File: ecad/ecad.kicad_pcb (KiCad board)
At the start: 2 copper layers, 0 parts

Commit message: chore (ecad): init PCB & Schematic
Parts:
- added U1: ESP32-CAM, boards:ESP32-CAM-DEVKIT, F.Cu at (63.5, 96.0)
- added U2: ESP32-WROOM-32, boards:ESP32-DEVKIT_CH340C, F.Cu at (70.0, 88.5)
- added U3: ESP32-WROOM-32, boards:ESP32-DEVKIT_CP2102, F.Cu at (76.5, 88.0)
- added U4: ESP32-S3, boards:ESP32-S3-DEVKIT_CH343p, F.Cu at (83.0, 86.0)

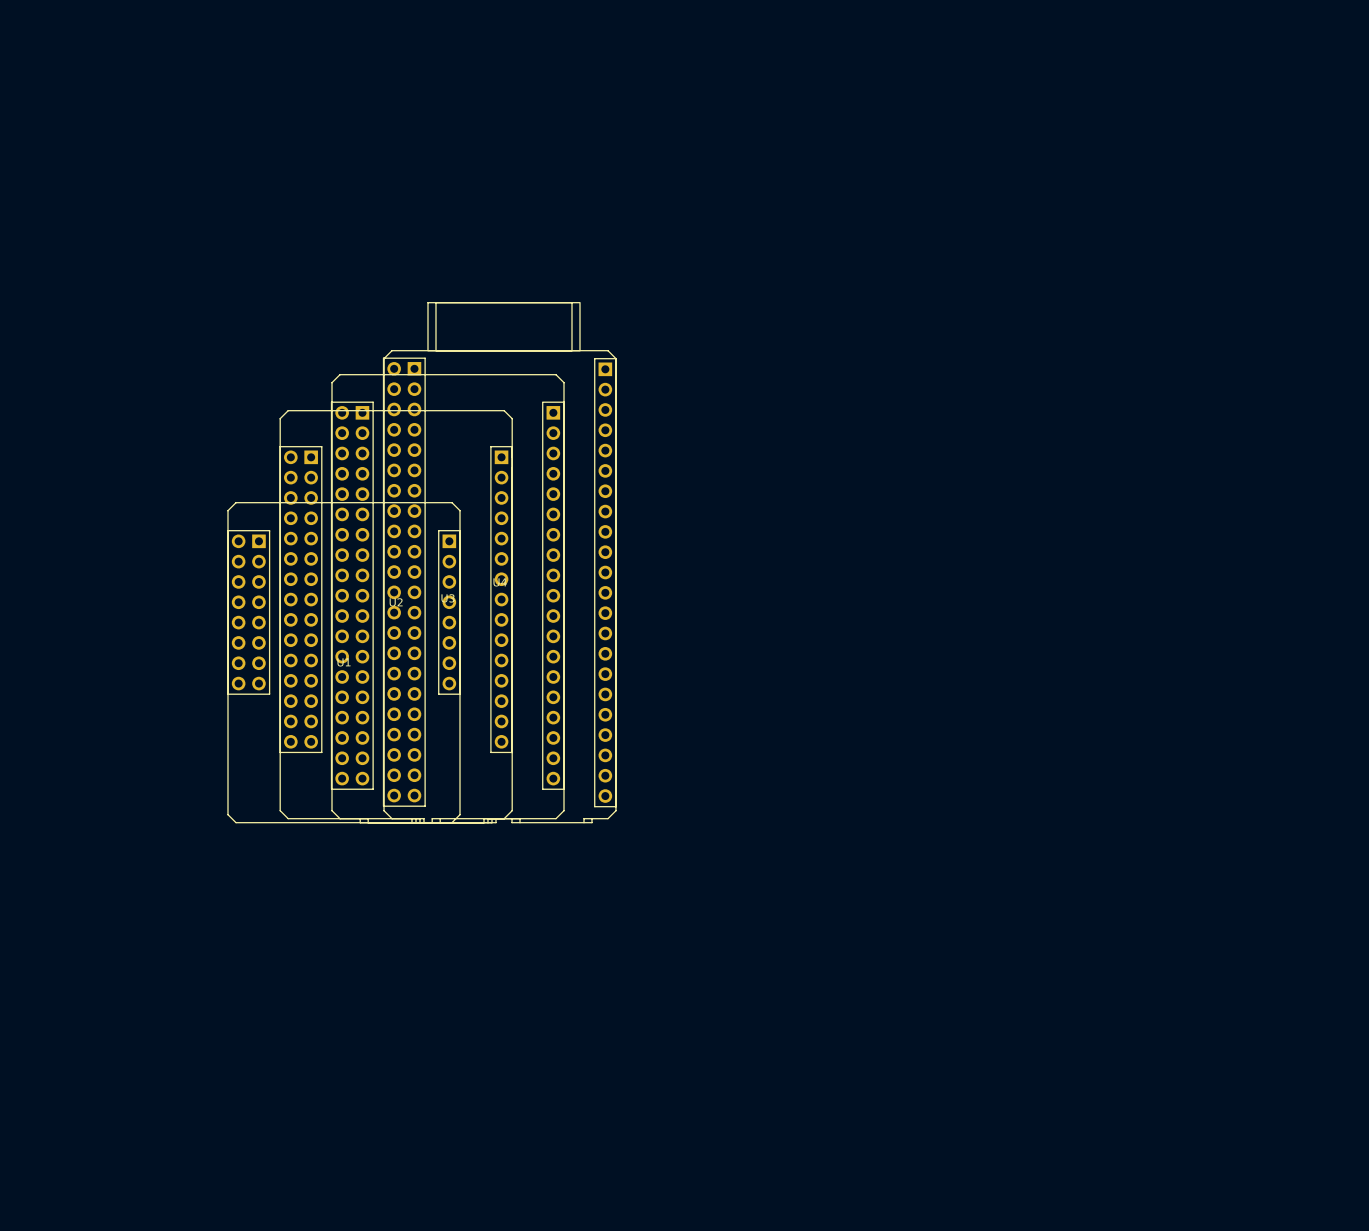
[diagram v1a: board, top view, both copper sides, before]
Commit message: feat (ecad): start PCB design
Left header pins and LEDs connected to devkits without ground-voltage
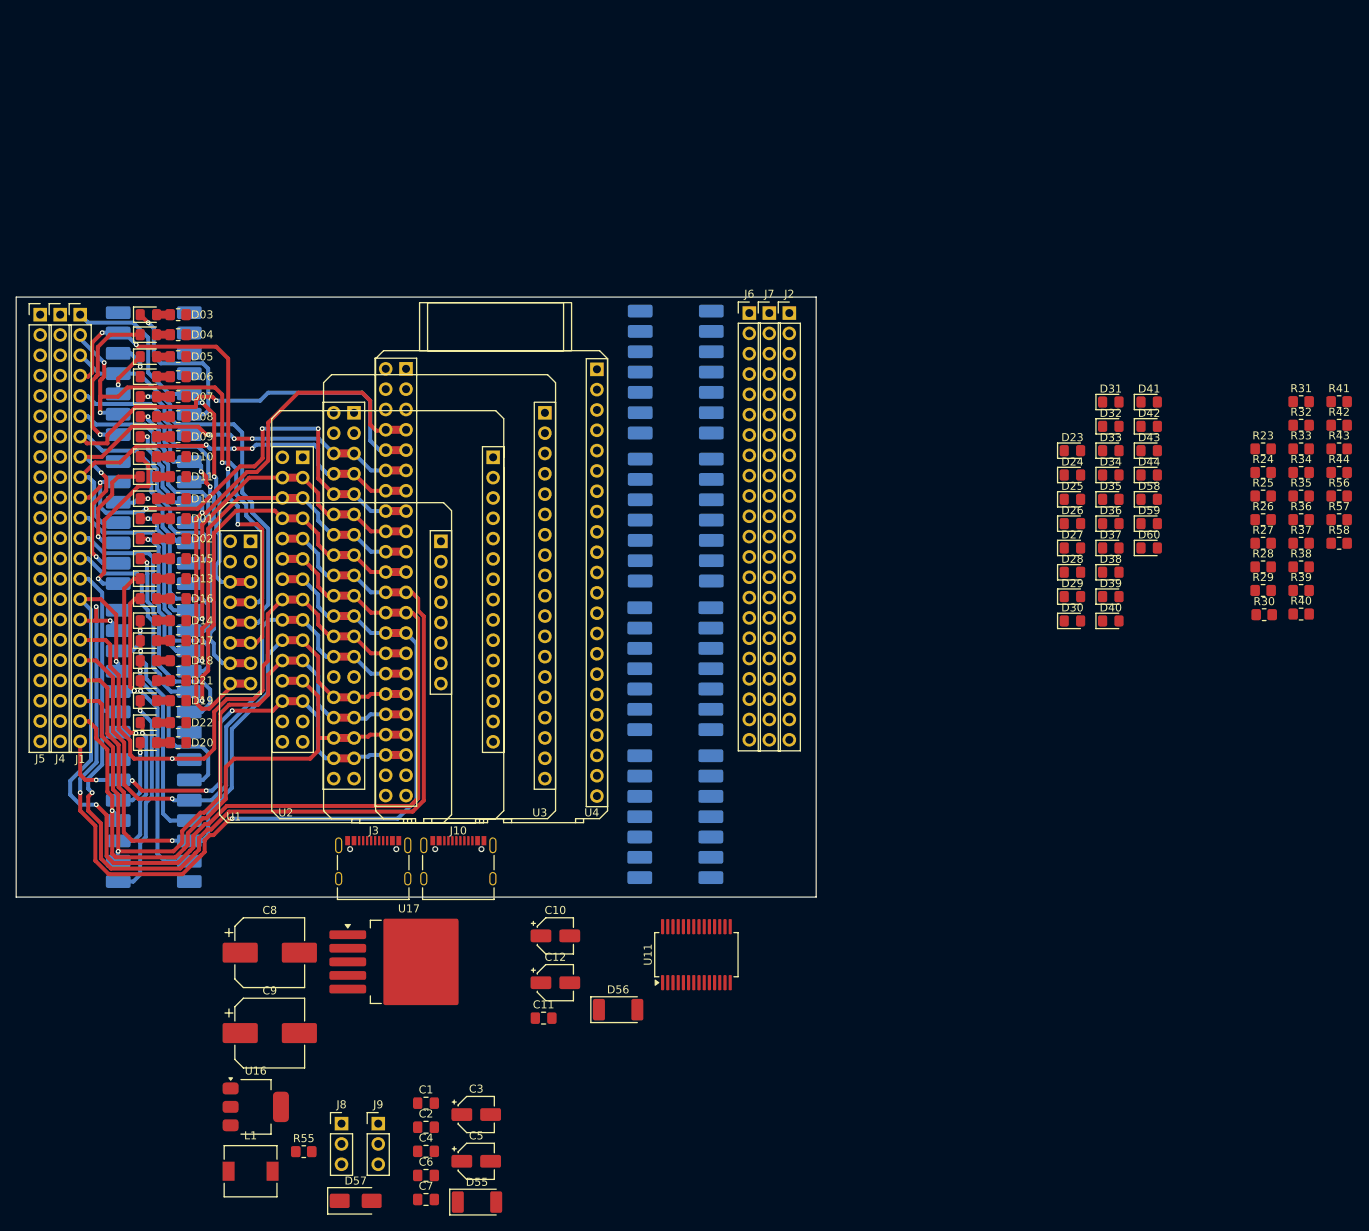
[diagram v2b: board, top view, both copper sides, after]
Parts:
- added C1: 100n, Capacitor_SMD:C_0805_2012Metric_Pad1.18x1.45mm_HandSolder, F.Cu at (73.7, 151.1)
- added C10: 1u, Capacitor_SMD:CP_Elec_4x5.4, F.Cu at (89.9, 130.2)
- added C11: 100n, Capacitor_SMD:C_0805_2012Metric_Pad1.18x1.45mm_HandSolder, F.Cu at (88.4, 140.4)
- added C12: 4.7u, Capacitor_SMD:CP_Elec_4x5.4, F.Cu at (89.9, 136.0)
- added C2: 100n, Capacitor_SMD:C_0805_2012Metric_Pad1.18x1.45mm_HandSolder, F.Cu at (73.7, 154.1)
- added C3: 1u, Capacitor_SMD:CP_Elec_4x5.4, F.Cu at (80.0, 152.5)
- added C4: 100n, Capacitor_SMD:C_0805_2012Metric_Pad1.18x1.45mm_HandSolder, F.Cu at (73.7, 157.1)
- added C5: 4.7u, Capacitor_SMD:CP_Elec_4x5.4, F.Cu at (80.0, 158.3)
- added C6: 22u, Capacitor_SMD:C_0805_2012Metric_Pad1.18x1.45mm_HandSolder, F.Cu at (73.7, 160.1)
- added C7: 22u, Capacitor_SMD:C_0805_2012Metric_Pad1.18x1.45mm_HandSolder, F.Cu at (73.7, 163.1)
- added C8: 470u, Capacitor_SMD:CP_Elec_8x10.5, F.Cu at (54.2, 132.2)
- added C9: 470u, Capacitor_SMD:CP_Elec_8x10.5, F.Cu at (54.2, 142.3)
- added D01: LED, LED_SMD:LED_0805_2012Metric_Pad1.15x1.40mm_HandSolder, F.Cu at (39.0, 78.0)
- added D02: LED, LED_SMD:LED_0805_2012Metric_Pad1.15x1.40mm_HandSolder, F.Cu at (39.0, 80.5)
- added D03: LED, LED_SMD:LED_0805_2012Metric_Pad1.15x1.40mm_HandSolder, F.Cu at (39.0, 52.5)
- added D04: LED, LED_SMD:LED_0805_2012Metric_Pad1.15x1.40mm_HandSolder, F.Cu at (39.0, 55.0)
- added D05: LED, LED_SMD:LED_0805_2012Metric_Pad1.15x1.40mm_HandSolder, F.Cu at (39.0, 57.8)
- added D06: LED, LED_SMD:LED_0805_2012Metric_Pad1.15x1.40mm_HandSolder, F.Cu at (39.0, 60.2)
- added D07: LED, LED_SMD:LED_0805_2012Metric_Pad1.15x1.40mm_HandSolder, F.Cu at (39.0, 62.8)
- added D08: LED, LED_SMD:LED_0805_2012Metric_Pad1.15x1.40mm_HandSolder, F.Cu at (39.0, 65.2)
- added D09: LED, LED_SMD:LED_0805_2012Metric_Pad1.15x1.40mm_HandSolder, F.Cu at (39.0, 67.8)
- added D10: LED, LED_SMD:LED_0805_2012Metric_Pad1.15x1.40mm_HandSolder, F.Cu at (39.0, 70.2)
- added D11: LED, LED_SMD:LED_0805_2012Metric_Pad1.15x1.40mm_HandSolder, F.Cu at (39.0, 72.8)
- added D12: LED, LED_SMD:LED_0805_2012Metric_Pad1.15x1.40mm_HandSolder, F.Cu at (39.0, 75.5)
- added D13: LED, LED_SMD:LED_0805_2012Metric_Pad1.15x1.40mm_HandSolder, F.Cu at (39.0, 85.5)
- added D14: LED, LED_SMD:LED_0805_2012Metric_Pad1.15x1.40mm_HandSolder, F.Cu at (39.0, 90.8)
- added D15: LED, LED_SMD:LED_0805_2012Metric_Pad1.15x1.40mm_HandSolder, F.Cu at (39.0, 83.0)
- added D16: LED, LED_SMD:LED_0805_2012Metric_Pad1.15x1.40mm_HandSolder, F.Cu at (39.0, 88.0)
- added D17: LED, LED_SMD:LED_0805_2012Metric_Pad1.15x1.40mm_HandSolder, F.Cu at (39.0, 93.2)
- added D18: LED, LED_SMD:LED_0805_2012Metric_Pad1.15x1.40mm_HandSolder, F.Cu at (39.0, 95.8)
- added D19: LED, LED_SMD:LED_0805_2012Metric_Pad1.15x1.40mm_HandSolder, F.Cu at (39.0, 100.8)
- added D20: LED, LED_SMD:LED_0805_2012Metric_Pad1.15x1.40mm_HandSolder, F.Cu at (39.0, 106.0)
- added D21: LED, LED_SMD:LED_0805_2012Metric_Pad1.15x1.40mm_HandSolder, F.Cu at (39.0, 98.2)
- added D22: LED, LED_SMD:LED_0805_2012Metric_Pad1.15x1.40mm_HandSolder, F.Cu at (39.0, 103.5)
- added D23: LED, LED_SMD:LED_0805_2012Metric_Pad1.15x1.40mm_HandSolder, F.Cu at (154.5, 69.5)
- added D24: LED, LED_SMD:LED_0805_2012Metric_Pad1.15x1.40mm_HandSolder, F.Cu at (154.5, 72.5)
- added D25: LED, LED_SMD:LED_0805_2012Metric_Pad1.15x1.40mm_HandSolder, F.Cu at (154.5, 75.6)
- added D26: LED, LED_SMD:LED_0805_2012Metric_Pad1.15x1.40mm_HandSolder, F.Cu at (154.5, 78.6)
- added D27: LED, LED_SMD:LED_0805_2012Metric_Pad1.15x1.40mm_HandSolder, F.Cu at (154.5, 81.7)
- added D28: LED, LED_SMD:LED_0805_2012Metric_Pad1.15x1.40mm_HandSolder, F.Cu at (154.5, 84.7)
- added D29: LED, LED_SMD:LED_0805_2012Metric_Pad1.15x1.40mm_HandSolder, F.Cu at (154.5, 87.7)
- added D30: LED, LED_SMD:LED_0805_2012Metric_Pad1.15x1.40mm_HandSolder, F.Cu at (154.5, 90.8)
- added D31: LED, LED_SMD:LED_0805_2012Metric_Pad1.15x1.40mm_HandSolder, F.Cu at (159.3, 63.4)
- added D32: LED, LED_SMD:LED_0805_2012Metric_Pad1.15x1.40mm_HandSolder, F.Cu at (159.3, 66.5)
- added D33: LED, LED_SMD:LED_0805_2012Metric_Pad1.15x1.40mm_HandSolder, F.Cu at (159.3, 69.5)
- added D34: LED, LED_SMD:LED_0805_2012Metric_Pad1.15x1.40mm_HandSolder, F.Cu at (159.3, 72.5)
- added D35: LED, LED_SMD:LED_0805_2012Metric_Pad1.15x1.40mm_HandSolder, F.Cu at (159.3, 75.6)
- added D36: LED, LED_SMD:LED_0805_2012Metric_Pad1.15x1.40mm_HandSolder, F.Cu at (159.3, 78.6)
- added D37: LED, LED_SMD:LED_0805_2012Metric_Pad1.15x1.40mm_HandSolder, F.Cu at (159.3, 81.7)
- added D38: LED, LED_SMD:LED_0805_2012Metric_Pad1.15x1.40mm_HandSolder, F.Cu at (159.3, 84.7)
- added D39: LED, LED_SMD:LED_0805_2012Metric_Pad1.15x1.40mm_HandSolder, F.Cu at (159.3, 87.7)
- added D40: LED, LED_SMD:LED_0805_2012Metric_Pad1.15x1.40mm_HandSolder, F.Cu at (159.3, 90.8)
- added D41: LED, LED_SMD:LED_0805_2012Metric_Pad1.15x1.40mm_HandSolder, F.Cu at (164.1, 63.4)
- added D42: LED, LED_SMD:LED_0805_2012Metric_Pad1.15x1.40mm_HandSolder, F.Cu at (164.1, 66.5)
- added D43: LED, LED_SMD:LED_0805_2012Metric_Pad1.15x1.40mm_HandSolder, F.Cu at (164.1, 69.5)
- added D44: LED, LED_SMD:LED_0805_2012Metric_Pad1.15x1.40mm_HandSolder, F.Cu at (164.1, 72.5)
- added D55: SM4001, Diode_SMD:D_MELF, F.Cu at (80.1, 163.4)
- added D56: SM4001, Diode_SMD:D_MELF, F.Cu at (97.7, 139.4)
- added D57: SS34, Diode_SMD:D_SMA, F.Cu at (64.9, 163.3)
- added D58: LED, LED_SMD:LED_0805_2012Metric_Pad1.15x1.40mm_HandSolder, F.Cu at (164.1, 75.6)
- added D59: LED, LED_SMD:LED_0805_2012Metric_Pad1.15x1.40mm_HandSolder, F.Cu at (164.1, 78.6)
- added D60: LED, LED_SMD:LED_0805_2012Metric_Pad1.15x1.40mm_HandSolder, F.Cu at (164.1, 81.7)
- added J1: Conn_01x22_Pin, Connector_PinHeader_2.54mm:PinHeader_1x22_P2.54mm_Vertical, F.Cu at (30.5, 52.5)
- added J10: USB_C, Connector_USB:USB_C_Receptacle_Palconn_UTC16-G, F.Cu at (77.8, 120.8)
- added J2: Conn_01x22_Pin, Connector_PinHeader_2.54mm:PinHeader_1x22_P2.54mm_Vertical, F.Cu at (119.1, 52.3)
- added J3: USB_C, Connector_USB:USB_C_Receptacle_Palconn_UTC16-G, F.Cu at (67.1, 120.8)
- added J4: Conn_01x22_Pin, Connector_PinHeader_2.54mm:PinHeader_1x22_P2.54mm_Vertical, F.Cu at (28.0, 52.5)
- added J5: Conn_01x22_Pin, Connector_PinHeader_2.54mm:PinHeader_1x22_P2.54mm_Vertical, F.Cu at (25.5, 52.5)
- added J6: Conn_01x22_Pin, Connector_PinHeader_2.54mm:PinHeader_1x22_P2.54mm_Vertical, F.Cu at (114.1, 52.3)
- added J7: Conn_01x22_Pin, Connector_PinHeader_2.54mm:PinHeader_1x22_P2.54mm_Vertical, F.Cu at (116.6, 52.3)
- added J8: Conn_01x03_Pin, Connector_PinHeader_2.54mm:PinHeader_1x03_P2.54mm_Vertical, F.Cu at (63.2, 153.6)
- added J9: Conn_01x03_Pin, Connector_PinHeader_2.54mm:PinHeader_1x03_P2.54mm_Vertical, F.Cu at (67.8, 153.6)
- added L1: 33u, Inductor_SMD:L_6.3x6.3_H3, F.Cu at (51.8, 159.6)
- added R01: 330, Resistor_SMD:R_0805_2012Metric_Pad1.20x1.40mm_HandSolder, F.Cu at (42.8, 78.0)
- added R02: 330, Resistor_SMD:R_0805_2012Metric_Pad1.20x1.40mm_HandSolder, F.Cu at (42.8, 80.5)
- added R03: 330, Resistor_SMD:R_0805_2012Metric_Pad1.20x1.40mm_HandSolder, F.Cu at (42.8, 52.5)
- added R04: 330, Resistor_SMD:R_0805_2012Metric_Pad1.20x1.40mm_HandSolder, F.Cu at (42.8, 55.0)
- added R05: 330, Resistor_SMD:R_0805_2012Metric_Pad1.20x1.40mm_HandSolder, F.Cu at (42.8, 57.8)
- added R06: 330, Resistor_SMD:R_0805_2012Metric_Pad1.20x1.40mm_HandSolder, F.Cu at (42.8, 60.2)
- added R07: 330, Resistor_SMD:R_0805_2012Metric_Pad1.20x1.40mm_HandSolder, F.Cu at (42.8, 62.8)
- added R08: 330, Resistor_SMD:R_0805_2012Metric_Pad1.20x1.40mm_HandSolder, F.Cu at (42.8, 65.2)
- added R09: 330, Resistor_SMD:R_0805_2012Metric_Pad1.20x1.40mm_HandSolder, F.Cu at (42.8, 67.8)
- added R10: 330, Resistor_SMD:R_0805_2012Metric_Pad1.20x1.40mm_HandSolder, F.Cu at (42.8, 70.2)
- added R11: 330, Resistor_SMD:R_0805_2012Metric_Pad1.20x1.40mm_HandSolder, F.Cu at (42.8, 72.8)
- added R12: 330, Resistor_SMD:R_0805_2012Metric_Pad1.20x1.40mm_HandSolder, F.Cu at (42.8, 75.5)
- added R13: 330, Resistor_SMD:R_0805_2012Metric_Pad1.20x1.40mm_HandSolder, F.Cu at (42.8, 85.5)
- added R14: 330, Resistor_SMD:R_0805_2012Metric_Pad1.20x1.40mm_HandSolder, F.Cu at (42.8, 90.8)
- added R15: 330, Resistor_SMD:R_0805_2012Metric_Pad1.20x1.40mm_HandSolder, F.Cu at (42.8, 83.0)
- added R16: 330, Resistor_SMD:R_0805_2012Metric_Pad1.20x1.40mm_HandSolder, F.Cu at (42.8, 88.0)
- added R17: 330, Resistor_SMD:R_0805_2012Metric_Pad1.20x1.40mm_HandSolder, F.Cu at (42.8, 93.2)
- added R18: 330, Resistor_SMD:R_0805_2012Metric_Pad1.20x1.40mm_HandSolder, F.Cu at (42.8, 95.8)
- added R19: 330, Resistor_SMD:R_0805_2012Metric_Pad1.20x1.40mm_HandSolder, F.Cu at (42.8, 100.8)
- added R20: 330, Resistor_SMD:R_0805_2012Metric_Pad1.20x1.40mm_HandSolder, F.Cu at (42.8, 106.0)
- added R21: 330, Resistor_SMD:R_0805_2012Metric_Pad1.20x1.40mm_HandSolder, F.Cu at (42.8, 98.2)
- added R22: 330, Resistor_SMD:R_0805_2012Metric_Pad1.20x1.40mm_HandSolder, F.Cu at (42.8, 103.5)
- added R23: 330, Resistor_SMD:R_0805_2012Metric_Pad1.20x1.40mm_HandSolder, F.Cu at (178.4, 69.3)
- added R24: 330, Resistor_SMD:R_0805_2012Metric_Pad1.20x1.40mm_HandSolder, F.Cu at (178.4, 72.2)
- added R25: 330, Resistor_SMD:R_0805_2012Metric_Pad1.20x1.40mm_HandSolder, F.Cu at (178.4, 75.2)
- added R26: 330, Resistor_SMD:R_0805_2012Metric_Pad1.20x1.40mm_HandSolder, F.Cu at (178.4, 78.1)
- added R27: 330, Resistor_SMD:R_0805_2012Metric_Pad1.20x1.40mm_HandSolder, F.Cu at (178.4, 81.1)
- added R28: 330, Resistor_SMD:R_0805_2012Metric_Pad1.20x1.40mm_HandSolder, F.Cu at (178.4, 84.0)
- added R29: 330, Resistor_SMD:R_0805_2012Metric_Pad1.20x1.40mm_HandSolder, F.Cu at (178.4, 87.0)
- added R30: 330, Resistor_SMD:R_0805_2012Metric_Pad1.20x1.40mm_HandSolder, F.Cu at (178.5, 90.0)
- added R31: 330, Resistor_SMD:R_0805_2012Metric_Pad1.20x1.40mm_HandSolder, F.Cu at (183.1, 63.4)
- added R32: 330, Resistor_SMD:R_0805_2012Metric_Pad1.20x1.40mm_HandSolder, F.Cu at (183.1, 66.3)
- added R33: 330, Resistor_SMD:R_0805_2012Metric_Pad1.20x1.40mm_HandSolder, F.Cu at (183.1, 69.3)
- added R34: 330, Resistor_SMD:R_0805_2012Metric_Pad1.20x1.40mm_HandSolder, F.Cu at (183.1, 72.2)
- added R35: 330, Resistor_SMD:R_0805_2012Metric_Pad1.20x1.40mm_HandSolder, F.Cu at (183.1, 75.2)
- added R36: 330, Resistor_SMD:R_0805_2012Metric_Pad1.20x1.40mm_HandSolder, F.Cu at (183.1, 78.1)
- added R37: 330, Resistor_SMD:R_0805_2012Metric_Pad1.20x1.40mm_HandSolder, F.Cu at (183.1, 81.1)
- added R38: 330, Resistor_SMD:R_0805_2012Metric_Pad1.20x1.40mm_HandSolder, F.Cu at (183.1, 84.0)
- added R39: 330, Resistor_SMD:R_0805_2012Metric_Pad1.20x1.40mm_HandSolder, F.Cu at (183.1, 87.0)
- added R40: 330, Resistor_SMD:R_0805_2012Metric_Pad1.20x1.40mm_HandSolder, F.Cu at (183.1, 89.9)
- added R41: 330, Resistor_SMD:R_0805_2012Metric_Pad1.20x1.40mm_HandSolder, F.Cu at (187.9, 63.4)
- added R42: 330, Resistor_SMD:R_0805_2012Metric_Pad1.20x1.40mm_HandSolder, F.Cu at (187.9, 66.3)
- added R43: 330, Resistor_SMD:R_0805_2012Metric_Pad1.20x1.40mm_HandSolder, F.Cu at (187.9, 69.3)
- added R44: 330, Resistor_SMD:R_0805_2012Metric_Pad1.20x1.40mm_HandSolder, F.Cu at (187.9, 72.2)
- added R55: 10k, Resistor_SMD:R_0805_2012Metric_Pad1.20x1.40mm_HandSolder, F.Cu at (58.4, 157.1)
- added R56: 330, Resistor_SMD:R_0805_2012Metric_Pad1.20x1.40mm_HandSolder, F.Cu at (187.9, 75.2)
- added R57: 1k, Resistor_SMD:R_0805_2012Metric_Pad1.20x1.40mm_HandSolder, F.Cu at (187.9, 78.1)
- added R58: 2k, Resistor_SMD:R_0805_2012Metric_Pad1.20x1.40mm_HandSolder, F.Cu at (187.9, 81.1)
- added U10: 4069, Package_DIP:DIP-14_W8.89mm_SMDSocket_LongPads, B.Cu at (104.9, 78.2)
- added U11: FT232RL, Package_SO:SSOP-28_5.3x10.2mm_P0.65mm, F.Cu at (107.5, 132.5)
- added U12: 4069, Package_DIP:DIP-14_W8.89mm_SMDSocket_LongPads, B.Cu at (104.9, 96.8)
- added U13: 4069, Package_DIP:DIP-14_W8.89mm_SMDSocket_LongPads, B.Cu at (104.9, 115.2)
- added U16: AMS1117-3.3, Package_TO_SOT_SMD:SOT-223-3_TabPin2, F.Cu at (52.4, 151.5)
- added U17: LM2596S-ADJ, Package_TO_SOT_SMD:TO-263-5_TabPin3, F.Cu at (71.6, 133.4)
- added U5: 4069, Package_DIP:DIP-14_W8.89mm_SMDSocket_LongPads, B.Cu at (39.7, 59.9)
- added U6: 4069, Package_DIP:DIP-14_W8.89mm_SMDSocket_LongPads, B.Cu at (39.7, 78.5)
- added U7: 4069, Package_DIP:DIP-14_W8.89mm_SMDSocket_LongPads, B.Cu at (39.7, 97.1)
- added U8: 4069, Package_DIP:DIP-14_W8.89mm_SMDSocket_LongPads, B.Cu at (39.7, 115.7)
- added U9: 4069, Package_DIP:DIP-14_W8.89mm_SMDSocket_LongPads, B.Cu at (104.9, 59.7)
- moved U2 1.06 mm to (68.9, 88.5)
- moved U1 1.05 mm to (62.4, 96.0)
- moved U3 1.05 mm to (75.4, 88.0)
- moved U4 1.05 mm to (81.9, 86.0)
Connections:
- U1 pad 1: unconnected-(U1-5V-Pad1) -> +5V
- U1 pad 10: unconnected-(U1-CLK3/TX0/GPIO01-Pad10) -> CAM_GPIO01
- U1 pad 11: unconnected-(U1-CLK2/RX0/GPIO03-Pad11) -> CAM_GPIO03
- U1 pad 12: unconnected-(U1-VCC-Pad12) -> +5V
- U1 pad 13: unconnected-(U1-GND-Pad13) -> Earth
- U1 pad 14: unconnected-(U1-CLK1/TOUCH1/ADC2_1/GPIO00-Pad14) -> CAM_GPIO00
- U1 pad 15: unconnected-(U1-RX2/GPIO16-Pad15) -> CAM_GPIO16
- U1 pad 16: unconnected-(U1-3V3-Pad16) -> +3.3V
- U1 pad 2: unconnected-(U1-GND-Pad2) -> Earth
- U1 pad 3: unconnected-(U1-GPIO12/ADC2_5/TOUCH5/DATA1-Pad3) -> CAM_GPIO12
- U1 pad 4: unconnected-(U1-GPIO13/ADC2_4/TOUCH4/DATA0-Pad4) -> CAM_GPIO13
- U1 pad 5: unconnected-(U1-GPIO15/ADC2_3/TOUCH3/CLK-Pad5) -> CAM_GPIO15
- U1 pad 6: unconnected-(U1-GPIO14/ADC2_6/TOUCH6/CMD-Pad6) -> CAM_GPIO14
- U1 pad 7: unconnected-(U1-GPIO02/ADC2_2/TOUCH2/DATA3-Pad7) -> CAM_GPIO02
- U1 pad 8: unconnected-(U1-GPIO04/ADC2_0/TOUCH0/DATA2-Pad8) -> CAM_GPIO04
- U1 pad 9: unconnected-(U1-GND-Pad9) -> Earth
- U2 pad 10: unconnected-(U2-GPIO27/ADC2_7/TOUCH7-Pad10) -> GPIO13_X38
- U2 pad 11: unconnected-(U2-GPIO14/ADC2_6/TOUCH6/HSPI_CLK-Pad11) -> FLASH_D2
- U2 pad 12: unconnected-(U2-GPIO12/ADC2_5/TOUCH5/HSPI_MISO-Pad12) -> FLASH_D3
- U2 pad 13: unconnected-(U2-GPIO13/ADC2_4/TOUCH4/HSPI_MOSI-Pad13) -> FLASH_CMD
- U2 pad 14: unconnected-(U2-GND-Pad14) -> Earth
- U2 pad 15: unconnected-(U2-VIN-Pad15) -> +5V
- U2 pad 16: unconnected-(U2-3V3-Pad16) -> +3.3V
- U2 pad 17: unconnected-(U2-GND-Pad17) -> Earth
- U2 pad 18: unconnected-(U2-HSPI_CS/TOUCH3/ADC2_3/GPIO15-Pad18) -> FLASH_SCK
- U2 pad 19: unconnected-(U2-CS/TOUCH2/ADC2_2/GPIO02-Pad19) -> FLASH_D0
- U2 pad 2: unconnected-(U2-GPIO36/ADC1_0/SENSOR_VP-Pad2) -> GPIO35_X38
- U2 pad 20: unconnected-(U2-TOUCH0/ADC2_0/GPIO04-Pad20) -> FLASH_D1
- U2 pad 21: unconnected-(U2-RX2/GPIO16-Pad21) -> GPIO15_X38
- U2 pad 22: unconnected-(U2-TX2/GPIO17-Pad22) -> GPIO02_X38
- U2 pad 23: unconnected-(U2-VSPI_CS/GPIO05-Pad23) -> GPIO00_X38
- U2 pad 24: unconnected-(U2-SCK/VSPI_CLK_/GPIO18-Pad24) -> GPIO04_X38
- U2 pad 25: unconnected-(U2-MISO/VSPI_MISO/GPIO19-Pad25) -> GPIO16_X38
- U2 pad 26: unconnected-(U2-SDA/GPIO21-Pad26) -> GPIO17_X38
- U2 pad 27: unconnected-(U2-CLK2/RX0/GPIO03-Pad27) -> GPIO03_X30
- U2 pad 28: unconnected-(U2-CLK3/TX0/GPIO01-Pad28) -> CAM_GPIO01
- U2 pad 29: unconnected-(U2-SCL/GPIO22-Pad29) -> GPIO19_X38
- U2 pad 3: unconnected-(U2-GPIO39/ADC1_3/SENSOR_VN-Pad3) -> GPIO32_X38
- U2 pad 30: unconnected-(U2-MOSI/VSPI_MOSI/GPIO23-Pad30) -> GPIO21_X38
- U2 pad 4: unconnected-(U2-GPIO34/ADC1_6-Pad4) -> GPIO33_X38
- U2 pad 5: unconnected-(U2-GPIO35/ADC1_7-Pad5) -> GPIO25_X38
- U2 pad 6: unconnected-(U2-GPIO32/ADC1_4/TOUCH9/XTAL32-Pad6) -> GPIO26_X38
- U2 pad 7: unconnected-(U2-GPIO33/ADC1_5/TOUCH8/XTAL32-Pad7) -> GPIO27_X38
- U2 pad 8: unconnected-(U2-GPIO25/ADC2_8/DAC1-Pad8) -> GPIO14_X38
- U2 pad 9: unconnected-(U2-GPIO26/ADC2_9/DAC2-Pad9) -> GPIO12_X38
- U3 pad 1: unconnected-(U3-3V3-Pad1) -> +3.3V
- U3 pad 10: unconnected-(U3-GPIO26/ADC2_9/DAC2-Pad10) -> GPIO26_X38
- U3 pad 11: unconnected-(U3-GPIO27/ADC2_7/TOUCH7-Pad11) -> GPIO27_X38
- U3 pad 12: unconnected-(U3-GPIO14/ADC2_6/TOUCH6/HSPI_CLK-Pad12) -> GPIO14_X38
- U3 pad 13: unconnected-(U3-GPIO12/ADC2_5/TOUCH5/HSPI_MISO-Pad13) -> GPIO12_X38
- U3 pad 14: unconnected-(U3-GND-Pad14) -> Earth
- U3 pad 15: unconnected-(U3-GPIO13/ADC2_4/TOUCH4/HSPI_MOSI-Pad15) -> GPIO13_X38
- U3 pad 16: unconnected-(U3-GPIO09/FLASH_D2/RX1-Pad16) -> FLASH_D2
- U3 pad 17: unconnected-(U3-GPIO10/FLASH_D3/TX1-Pad17) -> FLASH_D3
- U3 pad 18: unconnected-(U3-GPIO11/FLASH_CMD-Pad18) -> FLASH_CMD
- U3 pad 19: unconnected-(U3-5V-Pad19) -> +5V
- U3 pad 20: unconnected-(U3-FLASH_SCK/GPIO06-Pad20) -> FLASH_SCK
- U3 pad 21: unconnected-(U3-FLASH_D0/GPIO07-Pad21) -> FLASH_D0
- U3 pad 22: unconnected-(U3-FLASH_D1/GPIO08-Pad22) -> FLASH_D1
- U3 pad 23: unconnected-(U3-HSPI_CS/TOUCH3/ADC2_3/GPIO15-Pad23) -> GPIO15_X38
- U3 pad 24: unconnected-(U3-CS/TOUCH2/ADC2_2/GPIO02-Pad24) -> GPIO02_X38
- U3 pad 25: unconnected-(U3-TOUCH1/ADC2_1/GPIO00-Pad25) -> GPIO00_X38
- U3 pad 26: unconnected-(U3-TOUCH0/ADC2_0/GPIO04-Pad26) -> GPIO04_X38
- U3 pad 27: unconnected-(U3-RX2/GPIO16-Pad27) -> GPIO16_X38
- U3 pad 28: unconnected-(U3-TX2/GPIO17-Pad28) -> GPIO17_X38
- U3 pad 29: unconnected-(U3-VSPI_CS/GPIO05-Pad29) -> GPIO03_X30
- U3 pad 3: unconnected-(U3-GPIO36/ADC1_0/SENSOR_VP-Pad3) -> GPIO36_X38
- U3 pad 30: unconnected-(U3-SCK/VSPI_CLK_/GPIO18-Pad30) -> CAM_GPIO01
- U3 pad 31: unconnected-(U3-MISO/VSPI_MISO/GPIO19-Pad31) -> GPIO19_X38
- U3 pad 32: unconnected-(U3-GND-Pad32) -> Earth
- U3 pad 33: unconnected-(U3-SDA/GPIO21-Pad33) -> GPIO21_X38
- U3 pad 34: unconnected-(U3-CLK2/RX0/GPIO03-Pad34) -> GPIO03_X30
- U3 pad 35: unconnected-(U3-CLK3/TX0/GPIO01-Pad35) -> CAM_GPIO01
- U3 pad 36: unconnected-(U3-SCL/GPIO22-Pad36) -> CAM_GPIO01
- U3 pad 37: unconnected-(U3-MOSI/VSPI_MOSI/GPIO23-Pad37) -> CAM_GPIO03
- U3 pad 38: unconnected-(U3-GND-Pad38) -> Earth
- U3 pad 4: unconnected-(U3-GPIO39/ADC1_3/SENSOR_VN-Pad4) -> GPIO39_X38
- U3 pad 5: unconnected-(U3-GPIO34/ADC1_6-Pad5) -> GPIO34_X38
- U3 pad 6: unconnected-(U3-GPIO35/ADC1_7-Pad6) -> GPIO35_X38
- U3 pad 7: unconnected-(U3-GPIO32/ADC1_4/TOUCH9/XTAL32-Pad7) -> GPIO32_X38
- U3 pad 8: unconnected-(U3-GPIO33/ADC1_5/TOUCH8/XTAL32-Pad8) -> GPIO33_X38
- U3 pad 9: unconnected-(U3-GPIO25/ADC2_8/DAC1-Pad9) -> GPIO25_X38
- U4 pad 1: unconnected-(U4-3V3-Pad1) -> +3.3V
- U4 pad 10: unconnected-(U4-GPIO17/ADC2_6/TX1-Pad10) -> GPIO32_X38
- U4 pad 11: unconnected-(U4-GPIO18/ADC2_7/RX1/CLK3-Pad11) -> GPIO33_X38
- U4 pad 12: unconnected-(U4-GPIO08/ADC1_7/TOUCH8-Pad12) -> GPIO25_X38
- U4 pad 13: unconnected-(U4-GPIO03/ADC1_2/TOUCH3/JTAG-Pad13) -> GPIO26_X38
- U4 pad 14: unconnected-(U4-GPIO46/LOG-Pad14) -> GPIO27_X38
- U4 pad 15: unconnected-(U4-GPIO09/ADC1_8/TOUCH9-Pad15) -> GPIO14_X38
- U4 pad 16: unconnected-(U4-GPIO10/ADC1_9/TOUCH10-Pad16) -> GPIO12_X38
- U4 pad 17: unconnected-(U4-GPIO11/ADC2_0/TOUCH11-Pad17) -> GPIO13_X38
- U4 pad 18: unconnected-(U4-GPIO12/ADC2_1/TOUCH12-Pad18) -> FLASH_D2
- U4 pad 19: unconnected-(U4-GPIO13/ADC2_2/TOUCH13-Pad19) -> FLASH_D3
- U4 pad 2: unconnected-(U4-3V3-Pad2) -> +3.3V
- U4 pad 20: unconnected-(U4-GPIO14/ADC2_3/TOUCH14-Pad20) -> FLASH_CMD
- U4 pad 21: unconnected-(U4-5V-Pad21) -> +5V
- U4 pad 22: unconnected-(U4-GND-Pad22) -> Earth
- U4 pad 23: unconnected-(U4-GND-Pad23) -> Earth
- U4 pad 24: unconnected-(U4-GND-Pad24) -> Earth
- U4 pad 25: unconnected-(U4-USB-/RTS1/CLK2/ADC2_8/GPIO19-Pad25) -> FLASH_SCK
- U4 pad 26: unconnected-(U4-USB+/CTS1/CLK1/ADC2_9/GPIO20-Pad26) -> FLASH_D0
- U4 pad 27: unconnected-(U4-GPIO21-Pad27) -> FLASH_D1
- U4 pad 28: unconnected-(U4-SPICLK/GPIO47-Pad28) -> GPIO15_X38
- U4 pad 29: unconnected-(U4-SPICLK/GPIO48-Pad29) -> GPIO02_X38
- U4 pad 30: unconnected-(U4-VSPI/GPIO45-Pad30) -> GPIO00_X38
- U4 pad 31: unconnected-(U4-BOOT/GPIO0-Pad31) -> GPIO04_X38
- U4 pad 32: unconnected-(U4-SPIIO6/GPIO35-Pad32) -> GPIO16_X38
- U4 pad 33: unconnected-(U4-SPIIO7/GPIO36-Pad33) -> GPIO17_X38
- U4 pad 34: unconnected-(U4-SPIDQS/GPIO37-Pad34) -> GPIO03_X30
- U4 pad 35: unconnected-(U4-GPIO38-Pad35) -> CAM_GPIO01
- U4 pad 36: unconnected-(U4-MTCK/CLK3/GPIO39-Pad36) -> GPIO19_X38
- U4 pad 37: unconnected-(U4-MTDO/CLK2/GPIO40-Pad37) -> GPIO21_X38
- U4 pad 38: unconnected-(U4-MTDI/CLK1/GPIO41-Pad38) -> GPIO03_X30
- U4 pad 39: unconnected-(U4-MTMS/GPIO42-Pad39) -> CAM_GPIO01
- U4 pad 4: unconnected-(U4-GPIO04/ADC1_3/TOUCH4-Pad4) -> CAM_GPIO04
- U4 pad 40: unconnected-(U4-TOUCH2/ADC1_1/GPIO02-Pad40) -> GPIO22_X38
- U4 pad 41: unconnected-(U4-TOUCH1/ADC1_0/GPIO01-Pad41) -> GPIO23_X38
- U4 pad 42: unconnected-(U4-CLK2/RX0/GPIO44-Pad42) -> GPIO03_X30
- U4 pad 43: unconnected-(U4-CLK1/TX0/GPIO43-Pad43) -> CAM_GPIO01
- U4 pad 44: unconnected-(U4-GND-Pad44) -> Earth
- U4 pad 5: unconnected-(U4-GPIO05/ADC1_4/TOUCH5-Pad5) -> S3_GPIO05
- U4 pad 6: unconnected-(U4-GPIO06/ADC1_5/TOUCH6-Pad6) -> GPIO36_X38
- U4 pad 7: unconnected-(U4-GPIO07/ADC1_6/TOUCH7-Pad7) -> GPIO39_X38
- U4 pad 8: unconnected-(U4-GPIO15/ADC2_4/RTS0/XTAL32-Pad8) -> GPIO34_X38
- U4 pad 9: unconnected-(U4-GPIO16/ADC2_5/CTS0/XTAL32-Pad9) -> GPIO35_X38
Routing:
- net GPIO26_X38: track 0.00 -> 136.2 mm, vias 0 -> 2
- net GPIO25_X38: track 0.00 -> 132.1 mm, vias 0 -> 1
- net GPIO27_X38: track 0.00 -> 126.7 mm, vias 0 -> 4
- net CAM_GPIO04: track 0.00 -> 95.9 mm, vias 0 -> 1
- net FLASH_D2: track 0.00 -> 83.1 mm, vias 0 -> 1
- net GPIO13_X38: track 0.00 -> 82.7 mm, vias 0 -> 1
- net FLASH_D3: track 0.00 -> 79.7 mm, vias 0 -> 1
- net GPIO33_X38: track 0.00 -> 79.5 mm, vias 0 -> 1
- net GPIO12_X38: track 0.00 -> 77.5 mm, vias 0 -> 1
- net GPIO14_X38: track 0.00 -> 75.3 mm, vias 0 -> 1
- net S3_GPIO05: track 0.00 -> 73.9 mm, vias 0 -> 1
- net GPIO32_X38: track 0.00 -> 73.2 mm, vias 0 -> 1
- net GPIO35_X38: track 0.00 -> 67.9 mm, vias 0 -> 1
- net CAM_GPIO14: track 0.00 -> 67.7 mm, vias 0 -> 4
- net CAM_GPIO13: track 0.00 -> 64.1 mm, vias 0 -> 3
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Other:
- board outline added: 100 x 75 mm

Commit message: feat (ecad): update PCB design
header pins and LEDs connected to devkits without ground-voltage
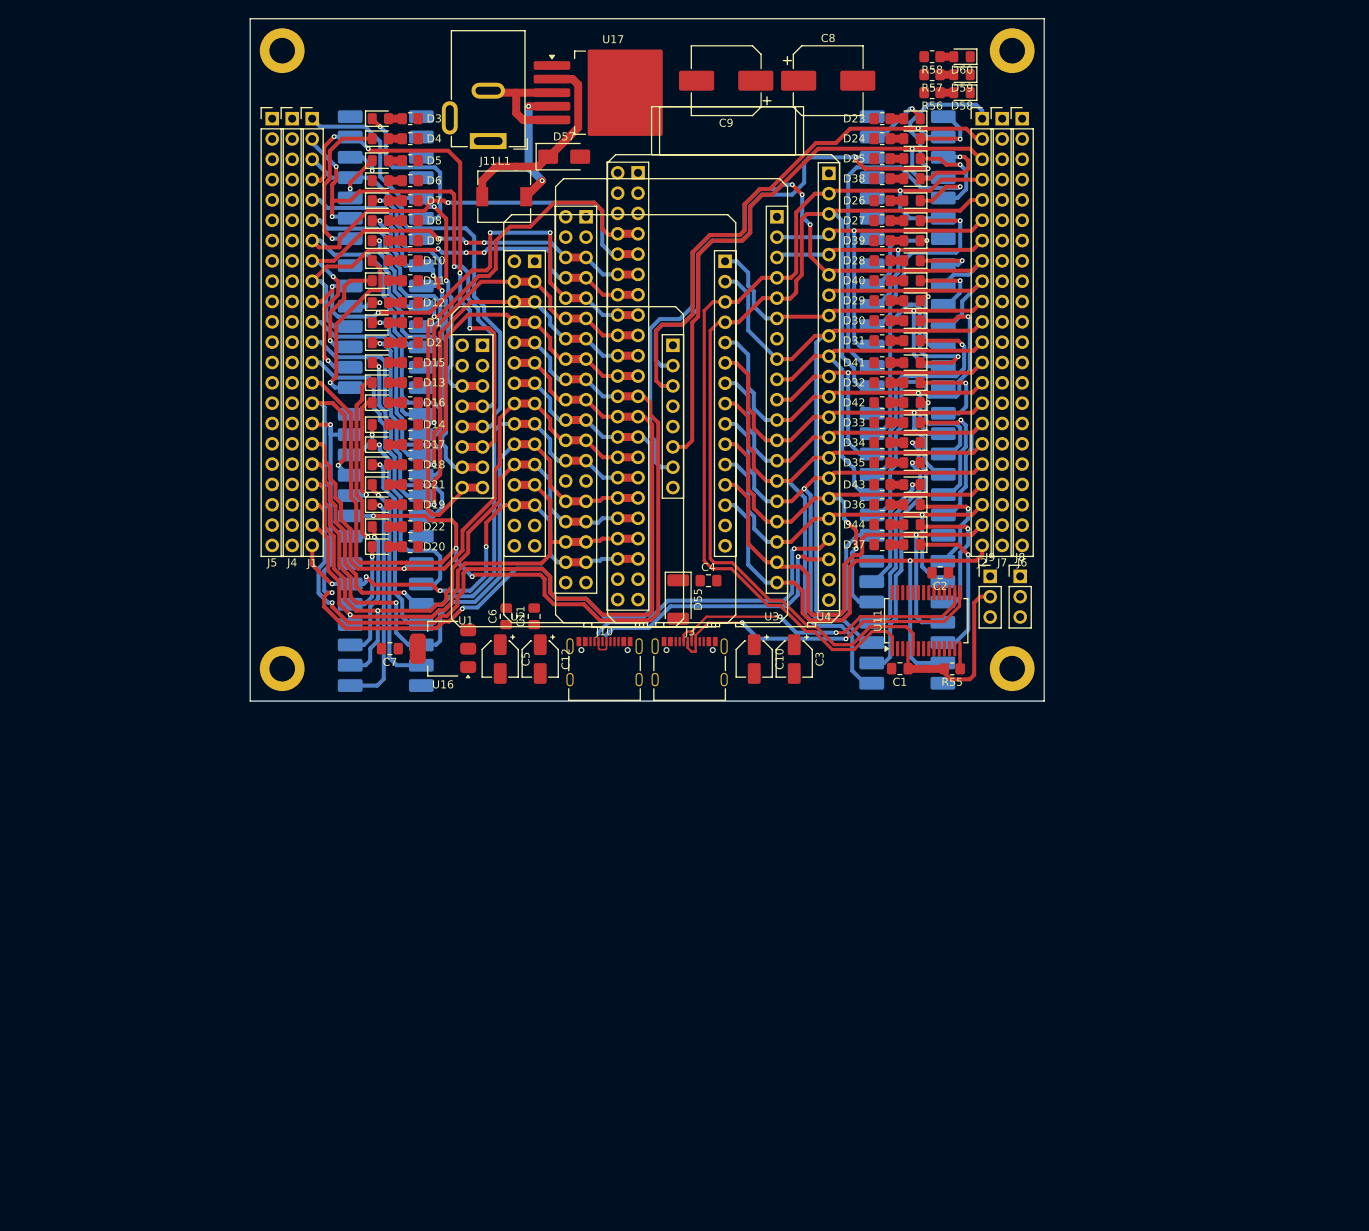
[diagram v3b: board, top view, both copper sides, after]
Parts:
- removed D56: SM4001, Diode_SMD:D_MELF
- added ?: , , F.Cu at (147.0, 19.5)
- added ?: , , F.Cu at (55.8, 96.8)
- added ?: , , F.Cu at (147.0, 96.8)
- added J11: Conn_01x02_Pin, Connector_BarrelJack:BarrelJack_GCT_DCJ200-10-A_Horizontal, F.Cu at (81.5, 30.8)
- added REF**: MountingHole_3.2mm_M3_DIN965_Pad, MountingHole:MountingHole_3.2mm_M3_DIN965_Pad, F.Cu at (55.8, 19.5)
- moved D57 133.1 mm to (91.0, 32.8)
- moved C9 132.0 mm to (111.2, 23.2), turned to 180 degrees
- moved C8 129.4 mm to (124.0, 23.2)
- moved L1 125.9 mm to (83.5, 37.8)
- moved U17 111.6 mm to (97.1, 24.8)
- moved J8 109.0 mm to (148.0, 85.2)
- moved J9 102.6 mm to (144.2, 85.2)
- moved R55 101.1 mm to (139.5, 96.8), turned to 180 degrees
- moved C2 94.5 mm to (138.0, 84.8), turned to 180 degrees
- moved C1 80.4 mm to (133.0, 96.8), turned to 180 degrees
- moved C4 79.6 mm to (109.0, 85.8)
- moved D55 79.4 mm to (105.2, 88.1), turned to -90 degrees
- moved R58 79.3 mm to (137.0, 20.2), turned to 180 degrees
- moved R57 75.4 mm to (137.0, 22.5), turned to 180 degrees
- moved R56 71.6 mm to (137.0, 24.8), turned to 180 degrees
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- renumbered D01 to D1, D02 to D2, D03 to D3, D04 to D4, D05 to D5, D06 to D6, D07 to D7, D08 to D8, D09 to D9, R01 to R1, R02 to R2, R03 to R3, R04 to R4, R05 to R5, R06 to R6, R07 to R7, R08 to R8, R09 to R9
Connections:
- J10 pad A6: FLASH_D0 -> S3_USB+
- J10 pad A7: FLASH_SCK -> S3_USB-
- J10 pad B6: FLASH_D0 -> S3_USB+
- J10 pad B7: FLASH_SCK -> S3_USB-
- J2 pad 12: CAM_GPIO01 -> GPIO18_X38
- J2 pad 13: GPIO03_X30 -> GPIO05_X38
- J2 pad 4: CAM_GPIO01 -> GPIO01_X30
- J2 pad 6: CAM_GPIO03 -> GPIO23_X38
- J2 pad 7: CAM_GPIO01 -> GPIO22_X38
- J2 pad 9: GPIO03_X30 -> S3_GPIO41
- U10 pad 1: CAM_GPIO01 -> GPIO03_X30
- U10 pad 11: GPIO22_X38 -> S3_GPIO41
- U10 pad 13: GPIO19_X38 -> GPIO21_X38
- U10 pad 3: CAM_GPIO01 -> GPIO23_X38
- U10 pad 5: GPIO03_X30 -> GPIO22_X38
- U10 pad 9: GPIO23_X38 -> CAM_GPIO01
- U11 pad 1: CAM_GPIO01 -> GPIO01_X30
- U12 pad 1: CAM_GPIO01 -> GPIO19_X38
- U12 pad 3: GPIO21_X38 -> GPIO18_X38
- U12 pad 5: GPIO19_X38 -> GPIO05_X38
- U13 pad 5: GPIO00_X38 -> GPIO15_X38
- U13 pad 9: GPIO02_X38 -> FLASH_D1
- U2 pad 28: CAM_GPIO01 -> GPIO01_X30
- U3 pad 29: GPIO03_X30 -> GPIO05_X38
- U3 pad 30: CAM_GPIO01 -> GPIO18_X38
- U3 pad 35: CAM_GPIO01 -> GPIO01_X30
- U3 pad 36: CAM_GPIO01 -> GPIO22_X38
- U3 pad 37: CAM_GPIO03 -> GPIO23_X38
- U4 pad 25: FLASH_SCK -> S3_USB-
- U4 pad 26: FLASH_D0 -> S3_USB+
- U4 pad 34: GPIO03_X30 -> GPIO05_X38
- U4 pad 35: CAM_GPIO01 -> GPIO18_X38
- U4 pad 38: GPIO03_X30 -> S3_GPIO41
- U4 pad 43: CAM_GPIO01 -> GPIO01_X30
- U9 pad 13: CAM_GPIO01 -> GPIO01_X30
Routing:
- net GPIO03_X30: track 0.00 -> 132.5 mm
- net GPIO01_X30: track 0.00 -> 116.1 mm, vias 0 -> 1
- net GPIO19_X38: track 0.00 -> 92.0 mm
- net CAM_GPIO01: track 0.00 -> 89.6 mm, vias 0 -> 3
- net CAM_GPIO16: track 0.00 -> 77.4 mm, vias 0 -> 2
- net CAM_GPIO03: track 0.00 -> 76.8 mm, vias 0 -> 1
- net GPIO00_X38: track 0.00 -> 74.8 mm
- net CAM_GPIO00: track 0.00 -> 70.8 mm, vias 0 -> 1
- net FLASH_D0: track 0.00 -> 67.7 mm, vias 0 -> 1
- net FLASH_SCK: track 0.00 -> 67.6 mm, vias 0 -> 1
- net GPIO02_X38: track 0.00 -> 66.5 mm, vias 0 -> 1
- net GPIO15_X38: track 0.00 -> 59.0 mm, vias 0 -> 2
- net GPIO04_X38: track 0.00 -> 56.3 mm
- net FLASH_D1: track 0.00 -> 51.3 mm, vias 0 -> 1
- net GPIO16_X38: track 0.00 -> 51.0 mm, vias 0 -> 1
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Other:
- board size 100 x 75 mm -> 99.2 x 85.3 mm
